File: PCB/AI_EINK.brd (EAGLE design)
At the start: 66 x 101.4 mm, 127 parts, among them J3 524372471, Q1 SI1308EDL-T1-GE3, T1 MMUN2133LT1G, U1 TPS61090RSAR, U2 MC74VHC1G14DFT1G, U3 BQ27441DRZR-G1A, U4 BQ24075, U5 TLV74328, U6 TLV74315, U7 TPA2005D1DRB

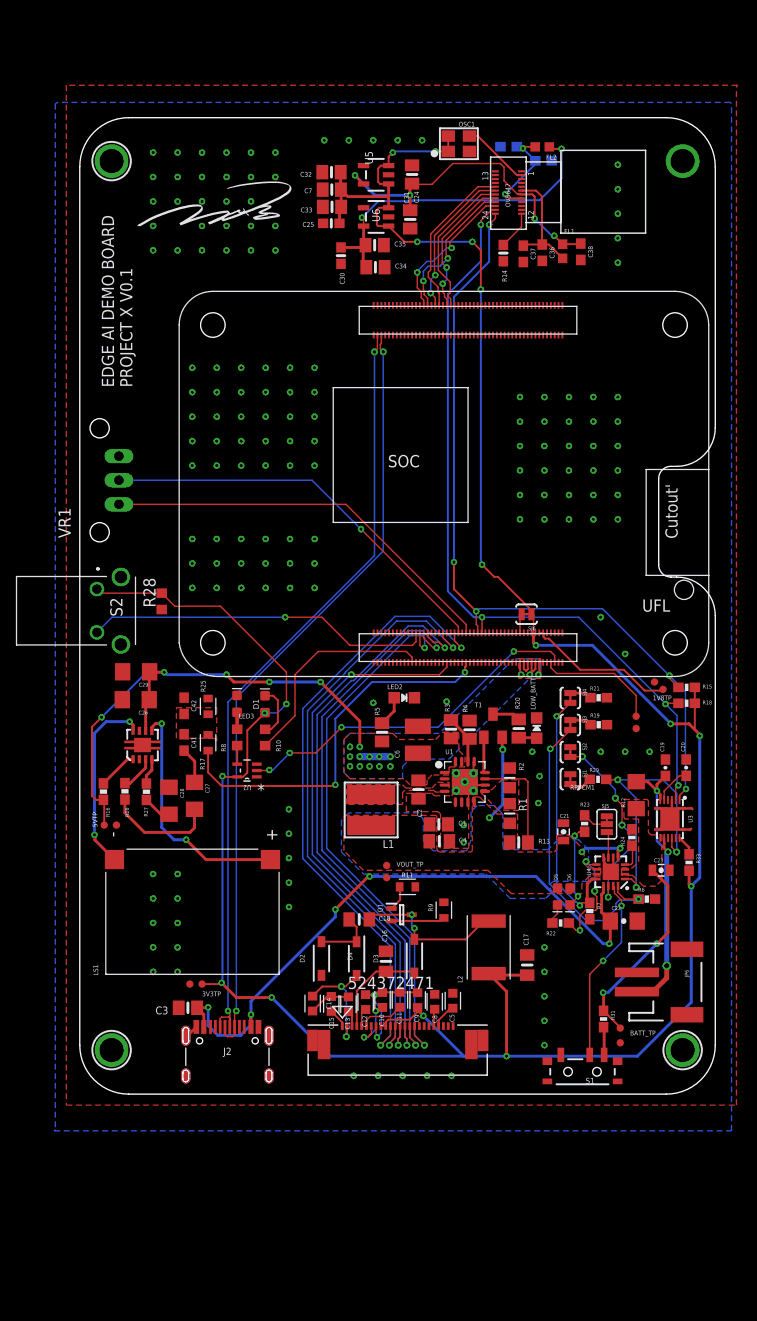
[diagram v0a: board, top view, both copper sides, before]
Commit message: added mic interface and RFID
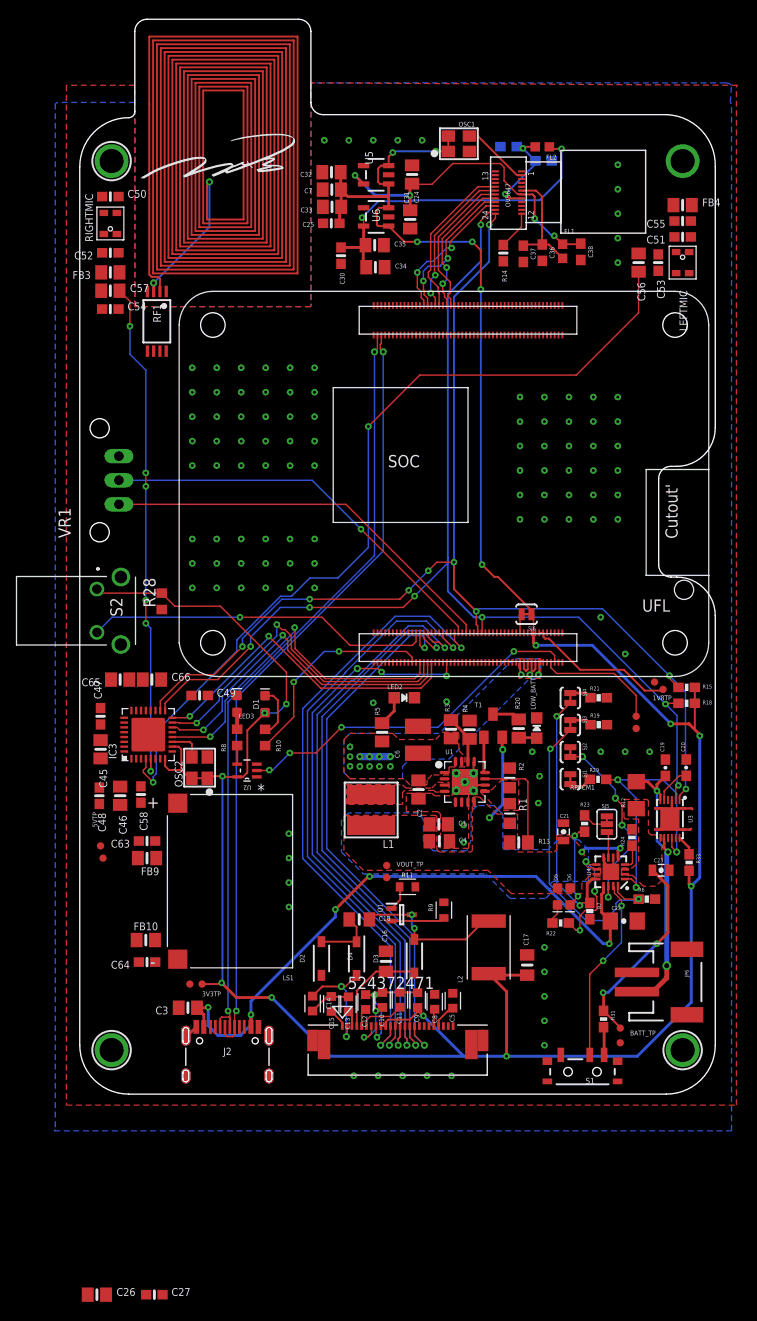
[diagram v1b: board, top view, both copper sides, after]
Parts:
- removed C28: 1uF, SparkFun:1206
- removed C29: 10uF, SparkFun:1206
- removed C41: 10uF, SparkFun-Capacitors:0603
- removed C42: 3.3nF, SparkFun-Capacitors:0603
- removed R16: 10K, SparkFun:0603-RES
- removed R17: 270R (ERJ-3EKF2700V), Resistor:RESC1608X60
- removed R25: 150R (CR0805J150RP05Z), Resistor:RESC1608X60
- removed R26, R27: 150K, SparkFun:0603-RES
- removed U7: TPA2005D1DRB, mike-temp:QFN-8_PAD
- added ANT1: NFC_ANTENNA_25X15, microbuilder:NFCANT_25X15
- added C45, C46, C56, C57, C65: 10uF, microbuilder:0805-NO
- added C47, C48, C49, C50, C51, C58: 0.1uF, microbuilder:0603-NO
- added C52, C53, C54, C55: 33pF, microbuilder:0603-NO
- added C63, C64: 100pF, microbuilder:0603-NO
- added C66: 2.2uF+, microbuilder:0805-NO
- added FB10, FB9: 120o, microbuilder:0805-NO
- added FB3: Ferrite, microbuilder:0805-NO
- added FB4: FERRITE, microbuilder:0805-NO
- added IC3: WM8960, microbuilder:QFN32_5MM
- added LEFTMIC, RIGHTMIC: (no value), microbuilder:SPW2430HR5H-B
- added OSC2: ECS-3225MV, microbuilder:OSC_3.2X2.5MM
- added RF1: ST25DVXX_TSSOP, microbuilder:TSSOP8-4.4MM
- C26: value 1uF -> 10uF; device SparkFun:1206 -> microbuilder:0805-NO
- C27: value 1uF -> 0.1uF; device SparkFun:1206 -> microbuilder:0603-NO
- moved C26 61.9 mm to (1.78, -20.8), turned to 0 degrees
- moved C27 52.0 mm to (7.75, -20.8), turned to 0 degrees
- moved LS1 5.03 mm to (15.6, 22.1), turned to 180 degrees
- moved GND13 3.70 mm to (2.41, 24.5)
- moved RPIBOOT1 2.19 mm to (2.16, 25.8)
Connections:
- net MCLK renamed RFC_MCLK
- removed net AUDIO: C27.1, C41.2
- removed net IN+AMP: R26.2, U7.3
- removed net IN-AMP: R27.2, U7.4
- removed net N$33: C28.2, R27.1
- removed net N$34: LS1.P, U7.5
- removed net N$35: LS1.N, U7.8
- removed net SDN*: R16.1, U7.1
- removed net SPEAKER: R17.1, RPI-CM1.49
- new net AGND: IC3.28, IC3.33
- new net AUDIO_MCLK: IC3.11, OSC2.3
- new net AVDD: C50.1, C51.1, C58.1, IC3.32, LEFTMIC.4, RIGHTMIC.4
- new net GPO: RF1.7
- new net I2S_BCLK: IC3.12, RPI-CM1.25
- new net I2S_DIN: IC3.16, RPI-CM1.31
- new net I2S_DOUT: IC3.14, RPI-CM1.29
- new net I2S_LRCLK: IC3.13, IC3.15, RPI-CM1.27
- new net LEFT_N: C64.1, FB10.2, LS1.N
- new net LEFT_P: C63.1, FB9.2, LS1.P
- new net LINPUT1: C56.2, IC3.4
- new net MICBIAS: C46.1, C48.1, IC3.1
- new net N$29: C52.1, FB3.1, RIGHTMIC.1
- new net N$31: C53.1, FB4.1, LEFTMIC.1
- new net N$36: C54.1, C57.1, FB3.2
- new net N$37: C55.1, C56.1, FB4.2
- new net N$40: FB9.1, IC3.25
- new net N$41: FB10.1, IC3.23
- new net RINPUT1: C57.2, IC3.5
- new net VEH: RF1.1
- new net VMID: C45.1, C47.1, IC3.27
- net 3.3V: now also C26.1, C27.1, C49.1, IC3.10, IC3.8, OSC2.1, OSC2.4, RF1.8
- net 5.0V: now also C65.1, C66.1, IC3.21, IC3.26; no longer C26.1, C29.1, R16.2, U7.6
- net GND: now also C27.2, C45.2, C46.2, C47.2, C48.2, C49.2, C50.2, C51.2, C52.2, C53.2, C54.2, C55.2, C58.2, C63.2, C64.2, C65.2, C66.2, IC3.20, IC3.24, IC3.9, LEFTMIC.2, LEFTMIC.3, OSC2.2, RF1.4, RIGHTMIC.2, RIGHTMIC.3; no longer C28.1, C29.2, C42.1, R25.1, U7.10, U7.11, U7.12, U7.13, U7.7
- net N$16: now also ANT1.P$2, RF1.2; no longer C41.1, C42.2, R17.2, R25.2
- net N$32: now also ANT1.P$1, RF1.3; no longer C27.2, R26.1
- net SCL: now also IC3.17, RF1.6
- net SDA: now also IC3.18, RF1.5
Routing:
- net LINPUT1: track 0.00 -> 88.8 mm, vias 0 -> 2
- net 5.0V: track 64.3 -> 10.4 mm, vias 20 -> 14
- net RINPUT1: track 0.00 -> 52.6 mm, vias 0 -> 6
- net SPEAKER: track 39.5 -> 0.00 mm, vias 2 -> 0
- net SDA: track 84.9 -> 122.8 mm, vias 5 -> 9
- net SCL: track 83.0 -> 120.2 mm, vias 4 -> 7
- net I2S_BCLK: track 0.00 -> 36.8 mm, vias 0 -> 2
- net I2S_LRCLK: track 0.00 -> 36.4 mm, vias 0 -> 2
- net I2S_DOUT: track 0.00 -> 36.2 mm, vias 0 -> 2
- net I2S_DIN: track 0.00 -> 34.8 mm, vias 0 -> 2
- net N$34: track 25.0 -> 0.00 mm, vias 2 -> 0
- net N$16: track 0.00 -> 20.3 mm
- net N$35: track 19.2 -> 0.00 mm, vias 2 -> 0
- net 3.3V: track 283.4 -> 293.9 mm
- net SDN*: track 4.13 -> 0.00 mm
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- removed copper zone on layer 1, net N$16
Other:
- board size 66 x 101.4 mm -> 66 x 111.6 mm

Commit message: bruh
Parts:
- moved C26 93.6 mm to (8.00, 72.5), turned to 180 degrees
- moved C27 91.4 mm to (8.00, 70.6), turned to 180 degrees
- moved GND13 30.5 mm to (29.2, 39.1)
- moved RPIBOOT1 29.2 mm to (29.2, 36.8)
- moved C50 7.11 mm to (3.05, 86.1)
- moved C52 7.11 mm to (3.05, 80.3)
- moved C54 7.11 mm to (3.05, 74.4)
- moved RIGHTMIC 7.11 mm to (3.05, 83.3)
- moved C57 7.11 mm to (3.05, 76.3)
- moved FB3 7.11 mm to (3.05, 78.2)
- moved C40 0.94 mm to (44.5, 99.3), flipped to the top, turned to 180 degrees
- moved LS1 0.52 mm to (15.5, 21.6)
- moved C39 0.09 mm to (48.1, 96.9), flipped to the top, turned to 0 degrees
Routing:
- net AVDD: track 0.00 -> 135.3 mm, vias 0 -> 11
- net 5.0V: track 10.4 -> 71.9 mm, vias 14 -> 16
- net 3.3V: track 293.9 -> 346.4 mm, vias 17 -> 19
- net SDA: track 122.8 -> 164.3 mm, vias 9 -> 11
- net SCL: track 120.2 -> 160.1 mm, vias 7 -> 9
- net N$41: track 0.00 -> 26.5 mm, vias 0 -> 2
- net N$40: track 0.00 -> 19.5 mm, vias 0 -> 2
- net N$37: track 0.00 -> 12.6 mm, vias 0 -> 2
- net N$31: track 0.00 -> 7.74 mm, vias 0 -> 2
- net LEFT_P: track 0.00 -> 6.16 mm
- net MICBIAS: track 0.00 -> 6.09 mm, vias 0 -> 2
- net RINPUT1: track 52.6 -> 46.7 mm, vias 6 -> 4
- net I2S_LRCLK: track 36.4 -> 41.2 mm, vias 2 -> 3
- net LEFT_N: track 0.00 -> 4.60 mm
- net VMID: track 0.00 -> 4.19 mm
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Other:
- board text added: "RPIBOOT"

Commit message: ditering
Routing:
- net 3.3V: track 346.4 -> 345.3 mm
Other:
- board text added: "/Users/chengmingzhang/Desktop/Screenshot_2024-02-21_at_10.06.41_PM.bmp"

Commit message: A
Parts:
- removed R31: 100k, SparkFun-Resistors:0603-RES
- removed SJ2, SJ3, SJ4: (no value), SparkFun-Passives:PAD-JUMPER-2-NC_BY_TRACE_YES_SILK
- added BOOST_EN, COUNTER_CLR, GND10, GND11, GND29, PULSE_555: TEST-POINT3, SparkFun-Connectors:PAD.03X.03
- added C28: 1uF, Capacitor:CAPC1608X85
- added C29, C41: 0.1uF, Capacitor:CAPC1608X85
- added C42: 0.1uF, microbuilder:0805_10MGAP
- added J1: BM04B-GHS-TBT(LF)(SN)(N), BM04B-GHS-TBT_LF__SN__N_:JST_BM04B-GHS-TBT(LF)(SN)(N)
- added OV5674: DF30FC-24DS-0.4V(82)CONN_DF30FC-24DS-0.4V(82)_HIR, 2024-03-07_05-07-01_Library:CONN_DF30FC-24DS-0.4V(82)_HIR
- added Q3: 2A/20V/150mΩ, SparkFun-DiscreteSemi:SOT26
- added R16: 280k, Resistor:RESC1608X60
- added R17, R25, R26, R27: 10k, Resistor:RESC1608X60
- added R30: 36k, Resistor:RESC1608X60
- added SW1: (no value), adafruit:PUSHBUTTON_SMD_SJ
- added U7: NE555DR, IC:SOIC-8N
- added U8: SN74LV4040ARGYRRGY16_2P55X2P05, 2024-03-07_02-24-03_Library:RGY16_2P55X2P05
- added U9: EMC2301-1-ACZL-TRMSOP8_MC_MCH-L, 2024-03-07_04-01-04_Library:MSOP8_MC_MCH-L
- C16: value 0.1uF -> 1uF
- C18: value 0.1uF -> 4.7uF
- R19: value 590 -> 10K; device SparkFun-Passives:0603-RES -> Resistor:RESC1608X60
- R21: value 1.1k -> 10k; device SparkFun-Passives:0603-RES -> Resistor:RESC1608X60
- moved R21 158.2 mm to (-3.75, -106.2)
- moved R19 148.6 mm to (-0.82, -99.8)
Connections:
- removed net N$24: R31.2, S1.1
- removed net N$26: R21.1, SJ4.1
- removed net N$27: R19.1, SJ3.1
- removed net N$30: C10.2, C11.2, C12.2, C9.2, J3.8
- removed net SYSOFF: S1.2, U4.15
- removed net TMR: SJ2.2, U4.14
- new net BOOST_EN: BOOST_EN.P$1, R13.1, S1.2, U8.5
- new net COUNTER_CLR: COUNTER_CLR.P$1, Q3.D2, R19.2, U8.11, U8.2
- new net FAN_PWM: J1.1, U9.5
- new net POWER_OFF_MCU: Q3.G2, RPI-CM1.41
- new net POWER_SWITCH_N: Q3.G1, R17.2, RPI-CM1.37, SW1.P$2
- new net PULSE_555: PULSE_555.P$1, U7.3, U8.10
- new net PWM_FAN: RPI-CM1.55
- new net TACH: J1.2, R30.1, U9.6
- new net TRIG: C28.1, R16.1, U7.2, U7.6
- new net V_OUT: Q3.S1, Q3.S2, S1.1, SW1.P$1, U8.16
- net 3.3V: now also R26.2, R27.2, R30.2, U9.3
- net 5.0V: now also C42.1, J1.3
- net GDR: now also Q1.1, R11.2
- net GND: now also C10.2, C11.2, C12.2, C13.2, C14.2, C15.2, C28.2, C29.2, C41.2, C42.2, C9.2, GND10.P$1, GND11.P$1, GND29.P$1, J1.4, J1.S1, J1.S2, J3.8, R17.1, R19.1, U4.14, U4.15, U7.1, U8.8, U9.4; no longer R19.2, R21.2, SJ2.1
- net ILIM: no longer SJ4.2
- net ISET: no longer SJ3.2
- net N$18: now also Q3.D1, R16.2, U7.4, U7.7, U7.8; no longer C13.2, C14.2, C15.2
- net N$20: now also R21.2, R26.1, VR1.A; no longer Q1.2, R9.2
- net N$22: now also R25.2, R27.1, VR1.B; no longer Q1.1, R11.2
- net RESE: now also Q1.2, R9.2
- net ROT1: now also C41.1, R25.1; no longer VR1.B
- net ROT2: now also C29.1, R21.1; no longer VR1.A
- net SCL: now also U9.2
- net SDA: now also U9.1
- net VOUT: no longer R13.1
- net V_BATT: no longer R31.1
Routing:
- net ISET: track 32.2 -> 3.11 mm, vias 2 -> 0
- net ILIM: track 27.1 -> 3.26 mm, vias 2 -> 0
- net ROT2: track 42.1 -> 18.5 mm
- net TMR: track 19.9 -> 0.00 mm, vias 4 -> 0
- net SYSOFF: track 19.3 -> 0.00 mm, vias 2 -> 0
- net BOOST_EN: track 0.00 -> 19.1 mm, vias 0 -> 2
- net GND: track 18.0 -> 34.0 mm, vias 174 -> 177
- net N$30: track 11.6 -> 0.00 mm, vias 2 -> 0
- net ROT1: track 42.2 -> 36.0 mm
- net RESE: track 0.00 -> 5.56 mm
- net N$20: track 5.56 -> 0.00 mm
- net N$18: track 4.39 -> 0.00 mm
- net V_BATT: track 20.9 -> 16.6 mm
- net N$24: track 2.90 -> 0.00 mm
- net V_OUT: track 0.00 -> 2.82 mm
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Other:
- board text added: "Reveri H1 V1.0 © PamirAI Inc. 2024"
- board text removed: "EDGE AI DEMO BOARD PROJECT X V0.1"
